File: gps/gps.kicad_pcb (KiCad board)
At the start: 2 copper layers, 167 x 82.5 mm, 67 parts, among them J1 I2C/BATT_H, J12 ENC+RGB, J13 ENC+RGB, J2 I2C/BATT_S, J3 USB_pads, J4 BATT, J5 ESP, J7 USB_B_Micro, J9 USB_pads, SW1 RotaryEncoder_Switch, SW2 MSN22AFW01, U1 NEO-M9N, U10 24C32, U11 SN74LV1T34DBVRG4, U2 TPS613222ADBVR, U3 DFR0654, U4 HT16k33, U5 7seg_1x1_rgb, U6 7seg_1x1_rgb, U7 7seg_1x1_rgb, U8 KW4-804AGB

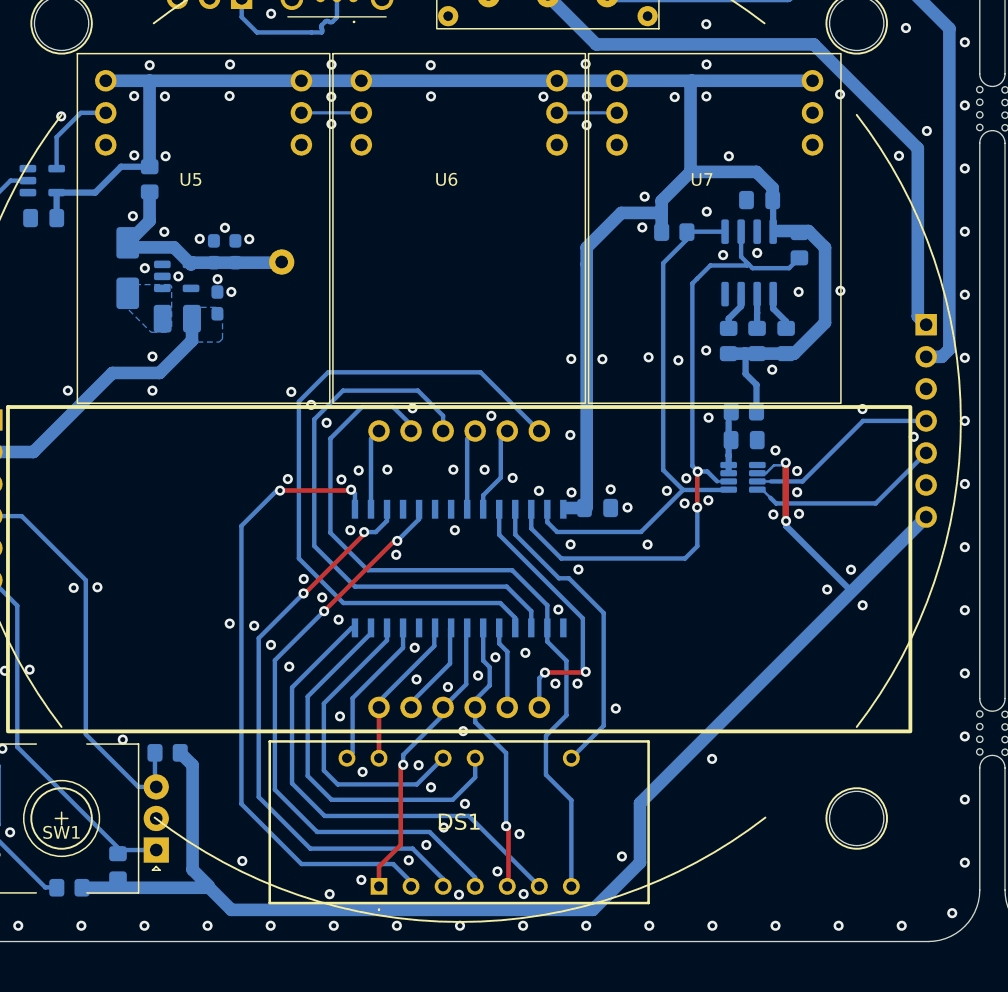
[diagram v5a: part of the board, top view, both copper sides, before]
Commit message: added pullup for 3V3 i2c
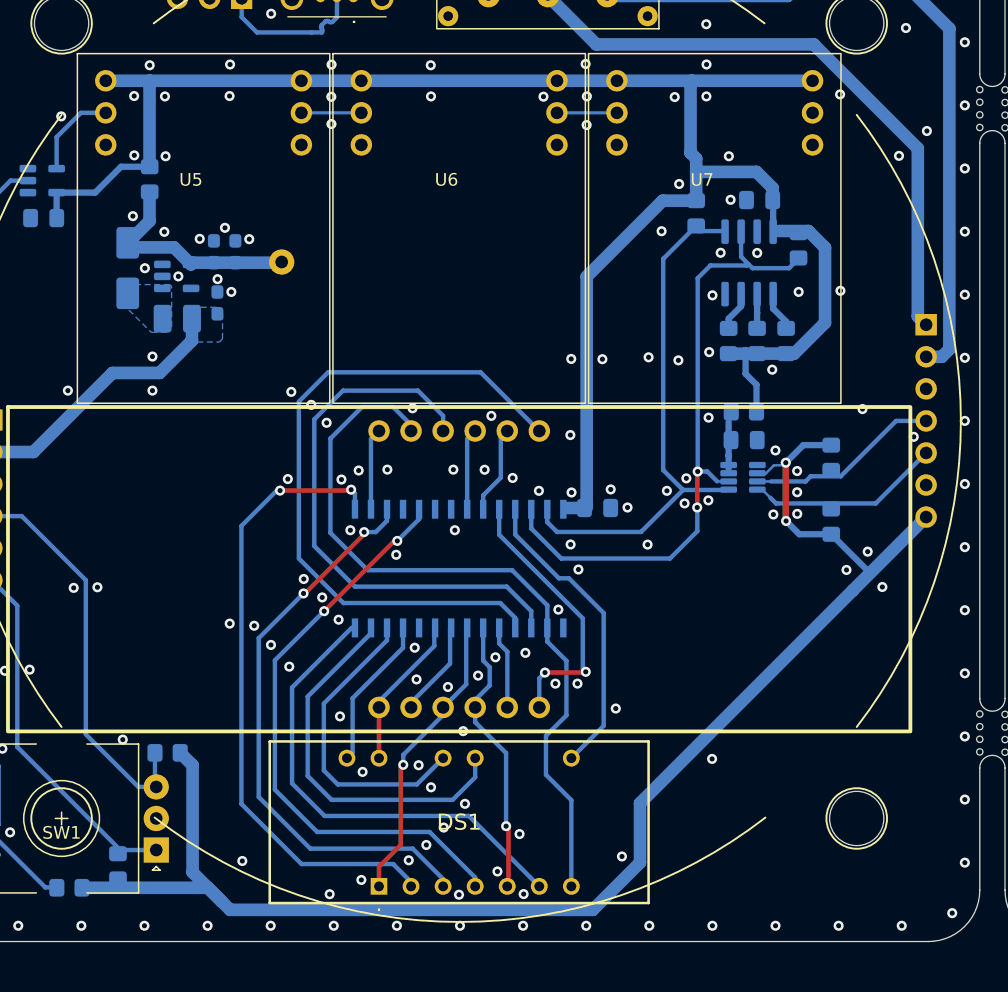
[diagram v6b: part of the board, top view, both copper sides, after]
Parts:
- removed R11, R12: 4k7, Resistor_SMD:R_0805_2012Metric_Pad1.20x1.40mm_HandSolder
- added R3: 4k7, Resistor_SMD:R_0805_2012Metric_Pad1.20x1.40mm_HandSolder, B.Cu at (112.8, 66.5)
- added R4: 4k7, Resistor_SMD:R_0805_2012Metric_Pad1.20x1.40mm_HandSolder, B.Cu at (120.9, 69.1)
- added R5: 4k7, Resistor_SMD:R_0805_2012Metric_Pad1.20x1.40mm_HandSolder, B.Cu at (123.5, 85.9)
- added R6: 4k7, Resistor_SMD:R_0805_2012Metric_Pad1.20x1.40mm_HandSolder, B.Cu at (123.5, 91.0)
- U9: value ~ -> TCA39306DDFR
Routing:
- net +3V3: track 179.8 -> 188.1 mm
- net +5V: track 150.2 -> 148.2 mm
- net SCL_5V: track 52.3 -> 51.2 mm
- net GND: vias 372 -> 373

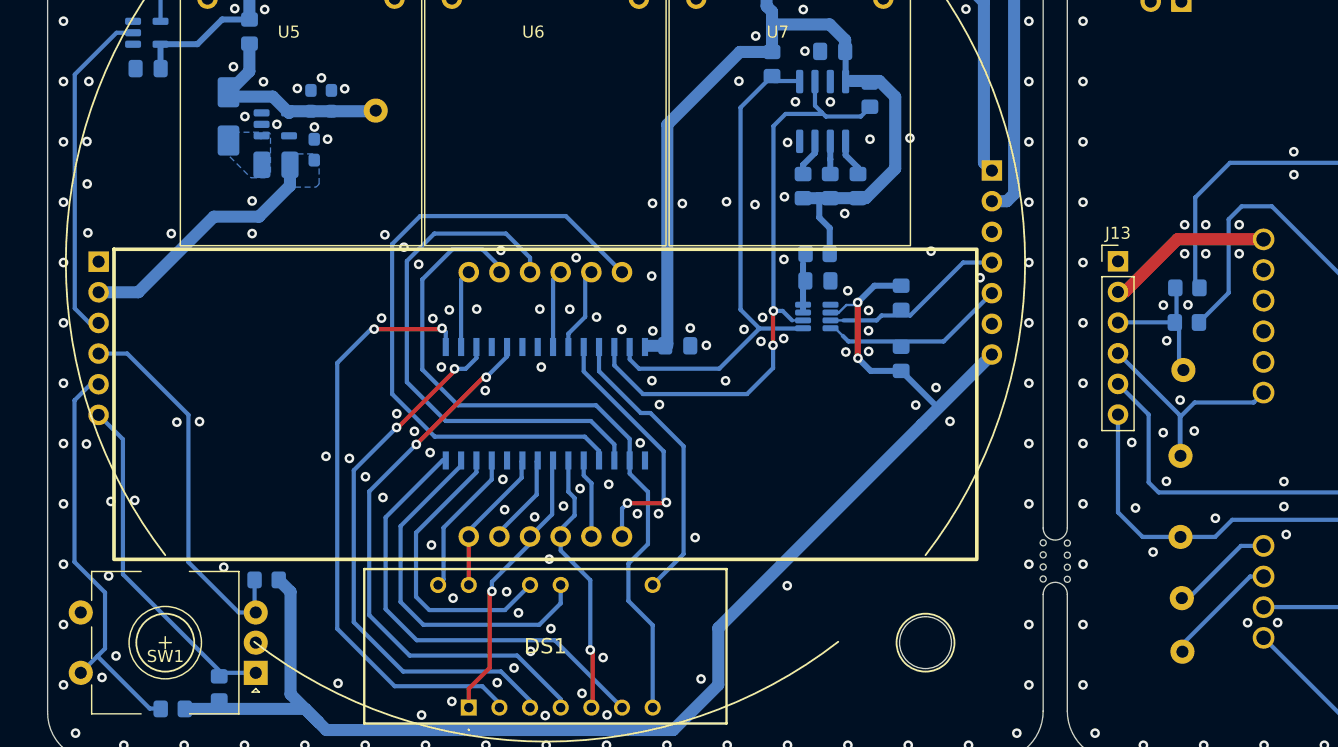
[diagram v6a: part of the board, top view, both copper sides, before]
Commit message: PCB - adjusted connectors to be inside circle (User.1)
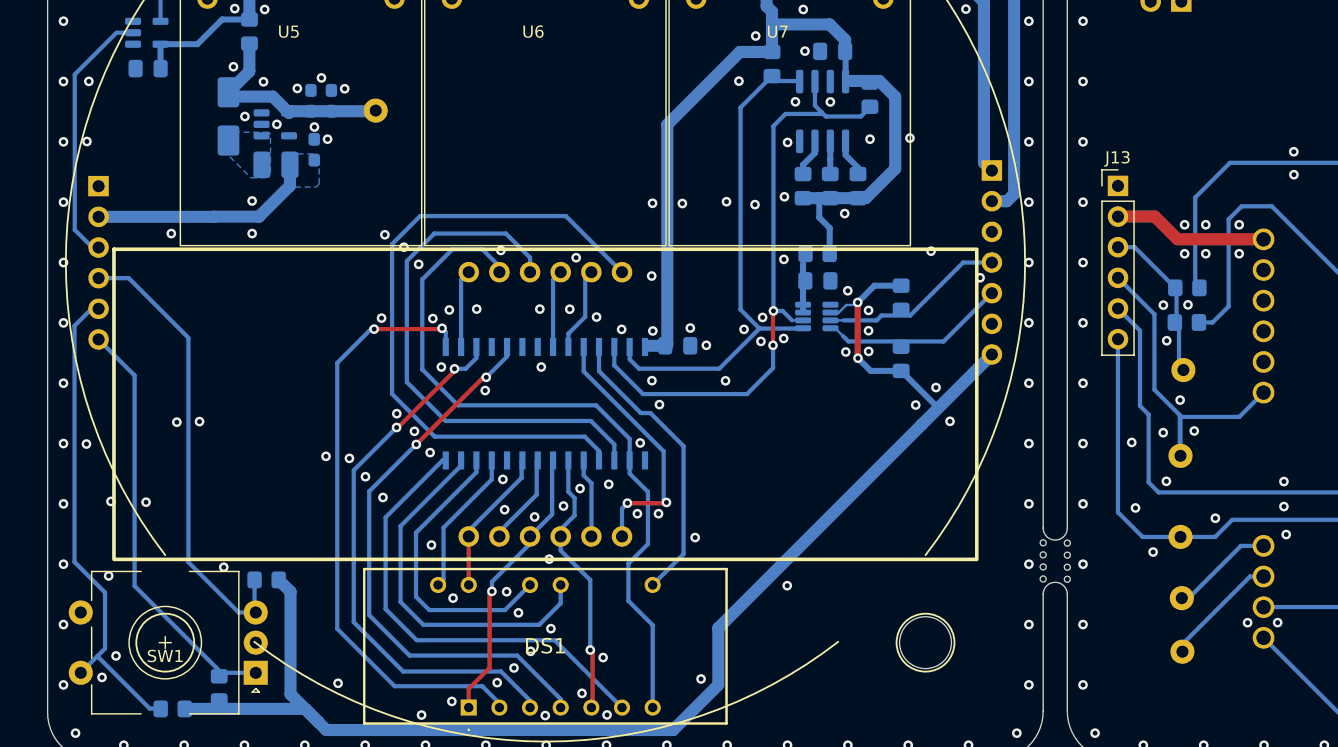
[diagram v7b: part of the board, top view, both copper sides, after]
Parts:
- moved J12 6.25 mm to (57.0, 76.7)
- moved J13 6.25 mm to (141.4, 76.7)
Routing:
- net DT: track 53.5 -> 66.1 mm
- net CLK: track 74.5 -> 87.0 mm
- net SW: track 77.5 -> 89.9 mm
- net RGB_3V3: track 40.4 -> 35.1 mm
- net VCC: track 35.1 -> 31.5 mm
- net Net-(U3-D7): track 45.3 -> 46.0 mm
- net GND: vias 373 -> 371

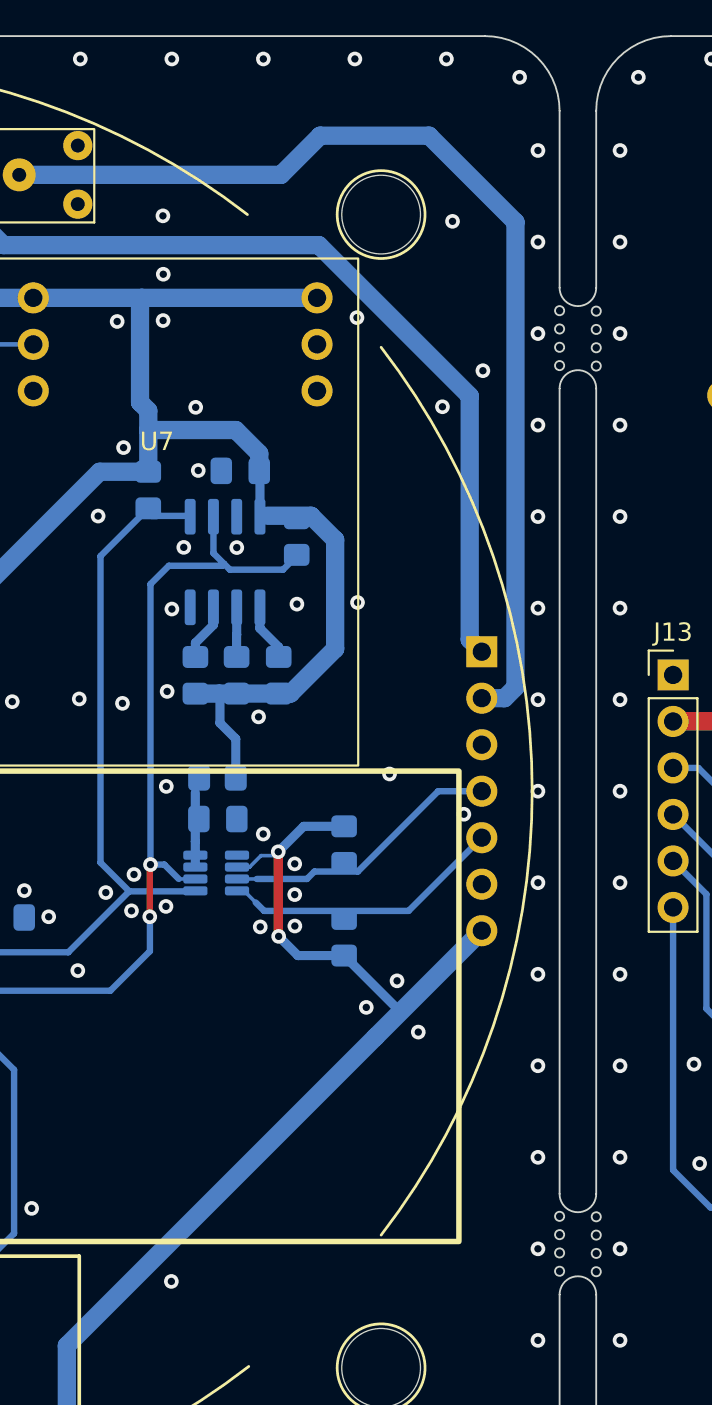
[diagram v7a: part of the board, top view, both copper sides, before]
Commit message: PCB - reworked mouse-bites
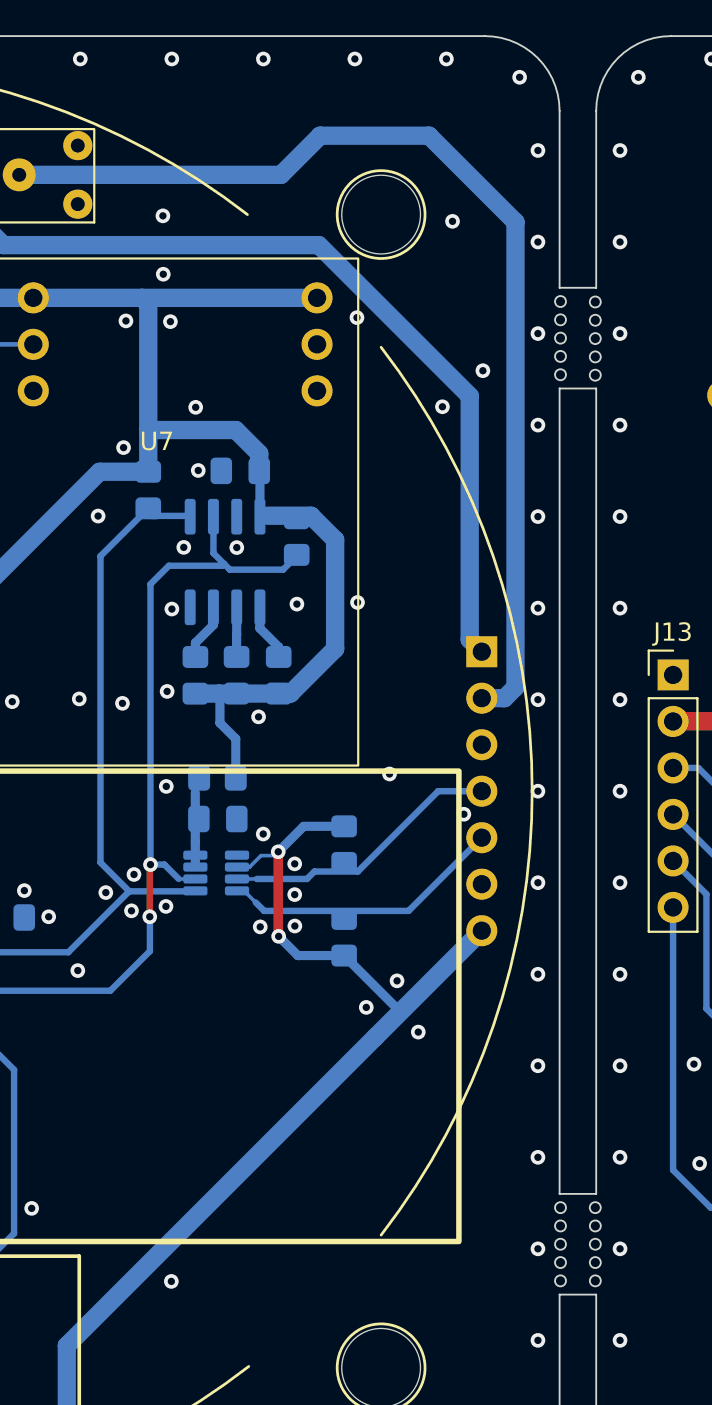
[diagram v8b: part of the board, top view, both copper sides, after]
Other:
- outline, holes or cut-outs redrawn
- board text added: "BOOT"
- board text added: "D+"
- board text added: "D-"
- board text added: "DM"
- board text added: "DP"
- board text added: "VBUS"
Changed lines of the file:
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@@
 		(tags "Through hole pin header THT 1x04 2.54mm single row")
 		(property "Reference" "J3"
-			(at 2.46 -5.3 90)
+			(at 2.23 -0.02 180)
 			(layer "B.SilkS")
 			(effects
@@
 		(tags "Connector")
 		(property "Reference" "J4"
-			(at -0.662 -3.794 90)
+			(at 0.09 -8.378 90)
 			(layer "B.SilkS")
 			(effects
@@
 	)
 	(gr_circle
-		(center 135.25 59.75)
-		(end 135.5 59.75)
+		(center 135.3 60.25)
+		(end 135.6 60.25)
 		(stroke
 			(width 0.1)
@@
 		(layer "Edge.Cuts")
 	)
-	(gr_arc
-		(start 137.25 105)
-		(mid 136.25 106)
-		(end 135.25 105)
+	(gr_line
+		(start 135.25 110.5)
+		(end 137.25 110.5)
 		(stroke
 			(width 0.1)
@@
 		(layer "Edge.Cuts")
 	)
+	(gr_circle
+		(center 137.2 105.75)
+		(end 137.5 105.75)
+		(stroke
+			(width 0.1)
+			(type default)
+		)
+		(fill none)
+		(layer "Edge.Cuts")
+	)
 	(gr_arc
 		(start 153.86 41.75)
@@
 	)
 	(gr_circle
-		(center 137.251976 58.775)
-		(end 137.501976 58.775)
+		(center 137.2 59.275)
+		(end 137.5 59.275)
 		(stroke
 			(width 0.1)
@@
 	)
 	(gr_circle
-		(center 135.25 56.75)
-		(end 135.5 56.75)
+		(center 135.3 57.25)
+		(end 135.6 57.25)
 		(stroke
 			(width 0.1)
@@
 	)
 	(gr_circle
-		(center 135.25 57.75)
-		(end 135.5 57.75)
+		(center 135.3 58.25)
+		(end 135.6 58.25)
 		(stroke
 			(width 0.1)
@@
 		(layer "Edge.Cuts")
 	)
+	(gr_line
+		(start 135.25 61)
+		(end 137.25 61)
+		(stroke
+			(width 0.1)
+			(type default)
+		)
+		(layer "Edge.Cuts")
+	)
 	(gr_arc
 		(start 219.75 120.171573)
@@
 	)
 	(gr_circle
-		(center 137.251976 57.775)
-		(end 137.501976 57.775)
+		(center 137.2 58.275)
+		(end 137.5 58.275)
 		(stroke
 			(width 0.1)
@@
 	)
 	(gr_circle
-		(center 135.25 108.225)
-		(end 135.5 108.225)
+		(center 135.3 108.75)
+		(end 135.6 108.75)
 		(stroke
 			(width 0.1)
@@
 	)
 	(gr_circle
-		(center 135.25 109.225)
-		(end 135.5 109.225)
+		(center 135.3 109.75)
+		(end 135.6 109.75)
 		(stroke
 			(width 0.1)
@@
 	)
 	(gr_circle
-		(center 137.251976 59.775)
-		(end 137.501976 59.775)
+		(center 137.2 60.275)
+		(end 137.5 60.275)
 		(stroke
 			(width 0.1)
@@
 	)
 	(gr_circle
-		(center 137.251976 106.25)
-		(end 137.501976 106.25)
+		(center 137.201976 106.75)
+		(end 137.501976 106.75)
 		(stroke
 			(width 0.1)
@@
 	)
 	(gr_circle
-		(center 137.251976 108.25)
-		(end 137.501976 108.25)
+		(center 137.201976 108.75)
+		(end 137.501976 108.75)
 		(stroke
 			(width 0.1)
@@
 	)
 	(gr_arc
-		(start 135.25 110.5)
-		(mid 136.25 109.5)
-		(end 137.25 110.5)
-		(stroke
-			(width 0.1)
-			(type default)
-		)
-		(layer "Edge.Cuts")
-	)
-	(gr_arc
 		(start 141.328427 124.25)
 		(mid 138.444535 123.055465)
@@
 	)
 	(gr_line
+		(start 135.25 55.5)
+		(end 137.25 55.5)
+		(stroke
+			(width 0.1)
+			(type default)
+		)
+		(layer "Edge.Cuts")
+	)
+	(gr_line
 		(start 141.328427 124.25)
 		(end 215.921573 124.25)
@@
 	)
 	(gr_circle
-		(center 135.25 106.225)
-		(end 135.5 106.225)
+		(center 135.3 106.75)
+		(end 135.6 106.75)
 		(stroke
 			(width 0.1)
@@
 	)
 	(gr_circle
-		(center 135.25 58.75)
-		(end 135.5 58.75)
+		(center 135.3 59.25)
+		(end 135.6 59.25)
 		(stroke
 			(width 0.1)
@@
 	)
 	(gr_circle
-		(center 137.251976 107.25)
-		(end 137.501976 107.25)
+		(center 137.201976 107.75)
+		(end 137.501976 107.75)
 		(stroke
 			(width 0.1)
@@
 	)
 	(gr_line
+		(start 135.25 105)
+		(end 137.25 105)
+		(stroke
+			(width 0.1)
+			(type default)
+		)
+		(layer "Edge.Cuts")
+	)
+	(gr_line
 		(start 135.25 45.828427)
 		(end 135.25 55.5)
@@
 		(layer "Edge.Cuts")
 	)
+	(gr_circle
+		(center 137.2 56.275)
+		(end 137.5 56.275)
+		(stroke
+			(width 0.1)
+			(type default)
+		)
+		(fill none)
+		(layer "Edge.Cuts")
+	)
 	(gr_arc
 		(start 172.2 45.75)
@@
 	)
 	(gr_line
-		(start 137.25 55.51)
+		(start 137.25 55.5)
 		(end 137.25 45.828427)
 		(stroke
@@
 	)
 	(gr_circle
-		(center 135.25 107.225)
-		(end 135.5 107.225)
+		(center 135.3 107.75)
+		(end 135.6 107.75)
 		(stroke
 			(width 0.1)
@@
 	)
 	(gr_circle
-		(center 137.251976 56.775)
-		(end 137.501976 56.775)
+		(center 137.2 57.275)
+		(end 137.5 57.275)
 		(stroke
 			(width 0.1)
@@
 		(layer "Edge.Cuts")
 	)
-	(gr_arc
-		(start 137.249999 55.51)
-		(mid 136.245 56.500036)
-		(end 135.249951 55.5)
+	(gr_circle
+		(center 135.3 105.75)
+		(end 135.6 105.75)
 		(stroke
 			(width 0.1)
 			(type default)
 		)
+		(fill none)
 		(layer "Edge.Cuts")
 	)
-	(gr_arc
-		(start 135.25 61)
-		(mid 136.25 60)
-		(end 137.25 61)
+	(gr_line
+		(start 137.25 120.171573)
+		(end 137.25 110.5)
 		(stroke
 			(width 0.1)
@@
 	)
 	(gr_line
-		(start 137.25 120.171573)
-		(end 137.25 110.5)
+		(start 171.2 46.75)
+		(end 155.87 46.75)
 		(stroke
 			(width 0.1)
@@
 		(layer "Edge.Cuts")
 	)
-	(gr_line
-		(start 171.2 46.75)
-		(end 155.87 46.75)
+	(gr_circle
+		(center 137.201976 109.75)
+		(end 137.501976 109.75)
 		(stroke
 			(width 0.1)
 			(type default)
 		)
+		(fill none)
 		(layer "Edge.Cuts")
 	)
 	(gr_circle
-		(center 137.251976 109.25)
-		(end 137.501976 109.25)
+		(center 135.3 56.25)
+		(end 135.6 56.25)
 		(stroke
 			(width 0.1)
@@
 		(layer "User.2")
 	)
+	(gr_text "D-"
+		(at 74.77 51.65 90)
+		(layer "B.SilkS")
+		(effects
+			(font
+				(size 1 1)
+				(thickness 0.15)
+			)
+			(justify left bottom mirror)
+		)
+	)
+	(gr_text "D+\n"
+		(at 77.59 51.57 90)
+		(layer "B.SilkS")
+		(effects
+			(font
+				(size 1 1)
+				(thickness 0.15)
+			)
+			(justify left bottom mirror)
+		)
+	)
+	(gr_text "VBUS"
+		(at 72.25 51.22 90)
+		(layer "B.SilkS")
+		(effects
+			(font
+				(size 1 1)
+				(thickness 0.15)
+			)
+			(justify left bottom mirror)
+		)
+	)
 	(gr_text "+"
-		(at 144.07 72.34 180)
+		(at 148.03 60.05 -90)
+		(layer "B.SilkS")
+		(effects
+			(font
+				(size 1 1)
+				(thickness 0.15)
+			)
+			(justify left bottom mirror)
+		)
+	)
+	(gr_text "DM"
+		(at 212.25 91.5 90)
 		(layer "B.SilkS")
 		(effects
@@
 		)
 	)
+	(gr_text "BOOT"
+		(at 214.8 96.65 90)
+		(layer "B.SilkS")
+		(effects
+			(font
+				(size 0.8 0.8)
+				(thickness 0.125)
+			)
+			(justify left bottom mirror)
+		)
+	)
 	(gr_text "-"
 		(at 179.08 47.24 90)
@@
 	)
 	(gr_text "-"
-		(at 144.07 67.14 -90)
+		(at 142.83 60.05 0)
 		(layer "B.SilkS")
 		(effects
@@
 		)
 	)
+	(gr_text "DP"
+		(at 208.45 93.65 -90)
+		(layer "B.SilkS")
+		(effects
+			(font
+				(size 1 1)
+				(thickness 0.15)
+			)
+			(justify left bottom mirror)
+		)
+	)
 	(gr_text "Cut pro kabely\n|\nV\n"
 		(at 166 39.9 0)
@@
 	)
 	(via
-		(at 113.59 57.29)
+		(at 113.99 57.35)
 		(size 0.8)
 		(drill 0.4)
@@
 	)
 	(via
-		(at 111.08 57.34)
+		(at 111.56 57.31)
 		(size 0.8)
 		(drill 0.4)
@@
 	)
 	(segment
-		(start 112.33 56.15)
-		(end 112.43 56.05)
-		(width 1)
-		(layer "B.Cu")
-		(net 4)
-	)
-	(segment
 		(start 117.602906 77.67)
 		(end 117.605 77.667906)
@@
 	)
 	(segment
-		(start 112.78 62.21)
-		(end 112.33 61.76)
-		(width 1)
-		(layer "B.Cu")
-		(net 4)
-	)
-	(segment
 		(start 122.99 75.225)
 		(end 122.99 69.27)
@@
 	)
 	(segment
+		(start 112.78 56.4)
+		(end 112.78 63.29)
+		(width 1)
+		(layer "B.Cu")
+		(net 4)
+	)
+	(segment
 		(start 62.1075 66.92)
 		(end 62.1175 66.93)
@@
 	)
 	(segment
-		(start 112.33 56.15)
-		(end 112.33 61.76)
-		(width 1)
-		(layer "B.Cu")
-		(net 4)
-	)
-	(segment
 		(start 115.355 77.67)
 		(end 116.65 77.67)
@@
 	)
 	(segment
-		(start 112.78 63.29)
-		(end 112.78 62.21)
+		(start 112.43 56.05)
+		(end 112.78 56.4)
 		(width 1)
 		(layer "B.Cu")
